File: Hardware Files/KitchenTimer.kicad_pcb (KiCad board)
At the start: 2 copper layers, 72.5 x 56 mm, 54 parts, among them J1 Conn_01x04, J2 USB_B_Micro, J3 Mounting Hole, J4 Mounting Hole, J5 Mounting Hole, J6 Mounting Hole, Q1 P 1V 250uA 4A SOT-23, Q2 P 1V 250uA 4A SOT-23, Q3 P 1V 250uA 4A SOT-23, Q4 P 1V 250uA 4A SOT-23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

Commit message: fix shift register pin mapping and routing
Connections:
- U3 pad 14: Data -> ShiftRegister_1_overflow
- U3 pad 9: ShiftRegister_1_overflow -> ShiftRegister_2_overflow
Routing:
- net Data: track 63.8 -> 17.2 mm, vias 2 -> 1
- net ShiftRegister_1_overflow: track 45.8 -> 40.2 mm, vias 2 -> 0
- net GND: track 72.4 -> 75.0 mm, vias 11 -> 12
- net ESP_RX: track 27.9 -> 26.8 mm

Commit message: update layout
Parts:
- R12, R13, R14, R15, R16, R17, R18, R19: value R -> 10Ω 100mW 0603
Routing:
- net (no net): track 0.00 -> 8.74 mm
- net BTN_StartStop: track 97.1 -> 105.0 mm
- net BTN_Down: track 105.8 -> 113.8 mm
- net BTN_Up: track 62.2 -> 70.2 mm
- net BTN_ResetCountdown: track 99.6 -> 107.5 mm
- net +3V3: track 63.0 -> 60.8 mm, vias 10 -> 13
- net ESP_Enable: track 23.9 -> 24.4 mm

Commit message: update components
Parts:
- C10, C12: value 220nF 50V -> 220nF
- C13, C9: value 10uF ±10% 25V X5R -> 10uF
- J1: value Conn_01x04 -> 2.54mm 1x4
- J2: value USB_B_Micro -> MicroUSB
- R12, R13, R14, R15, R16, R17, R18, R19: value 10Ω 100mW 0603 -> 10Ω
- SW1, SW2: value SW_SPST -> SPST
- SW3, SW4, SW5, SW6: value SW_Push_Dual -> SPST
- U2, U3: value 74HC595 -> Serial to Parallel Shift Register
- U4: value NCP1117ST33T3G -> 3.3 V Linear Regulator

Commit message: finalize layout
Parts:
- added G***: LOGO, .[--Stasis.Footprints.Library:PCBA Revision, B.Cu at (33.0, 70.8)
- added R20: 10Ω, Resistor_SMD:R_0603_1608Metric_Pad0.98x0.95mm_HandSolder, B.Cu at (63.0, 45.5)
- moved R18 5.00 mm to (63.0, 59.5)
- moved R14 4.80 mm to (63.0, 57.8)
- moved R19 4.60 mm to (63.0, 56.0)
- moved R15 4.41 mm to (63.0, 54.2)
- moved R16 4.22 mm to (63.0, 52.5)
- moved R12 4.03 mm to (63.0, 50.8)
- moved R17 3.85 mm to (63.0, 49.0)
- moved R13 3.67 mm to (63.0, 47.2)
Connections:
- LED1 pad 8: GND -> Net-(LED1-Pad8)
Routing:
- net +3V3: track 60.8 -> 51.6 mm, vias 13 -> 15
- net Net-(LED1-Pad8): track 0.00 -> 7.07 mm
- net Net-(LED1-Pad13): track 19.0 -> 24.3 mm
- net Net-(LED1-Pad12): track 15.3 -> 20.1 mm
- net Net-(LED1-Pad9): track 6.41 -> 10.8 mm
- net BTN_ResetCountdown: track 107.5 -> 111.2 mm
- net GND: track 75.0 -> 71.4 mm, vias 12 -> 15
- net LED_G: track 32.0 -> 34.4 mm
- net LED_C: track 21.6 -> 23.8 mm
- net LED_B: track 5.11 -> 7.32 mm
- net LED_DP: track 18.6 -> 20.7 mm
- net Net-(LED1-Pad5): track 9.46 -> 11.3 mm
- net LED_F: track 7.75 -> 9.60 mm
- net LED_A: track 10.4 -> 12.2 mm
- net LED_D: track 16.0 -> 17.8 mm
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- added copper zone on F.Cu, net +3V3
- added copper zone on B.Cu, net GND
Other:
- board text added: "5 V"
- board text added: "BOOT"
- board text added: "DOWN"
- board text added: "EN"
- board text added: "GND"
- board text added: "HR"
- board text added: "MIN"
- board text added: "RESET"
- board text added: "RX"
- board text added: "START"
- board text added: "STOP"
- board text added: "TIMER"
- board text added: "TX"
- board text added: "UP"

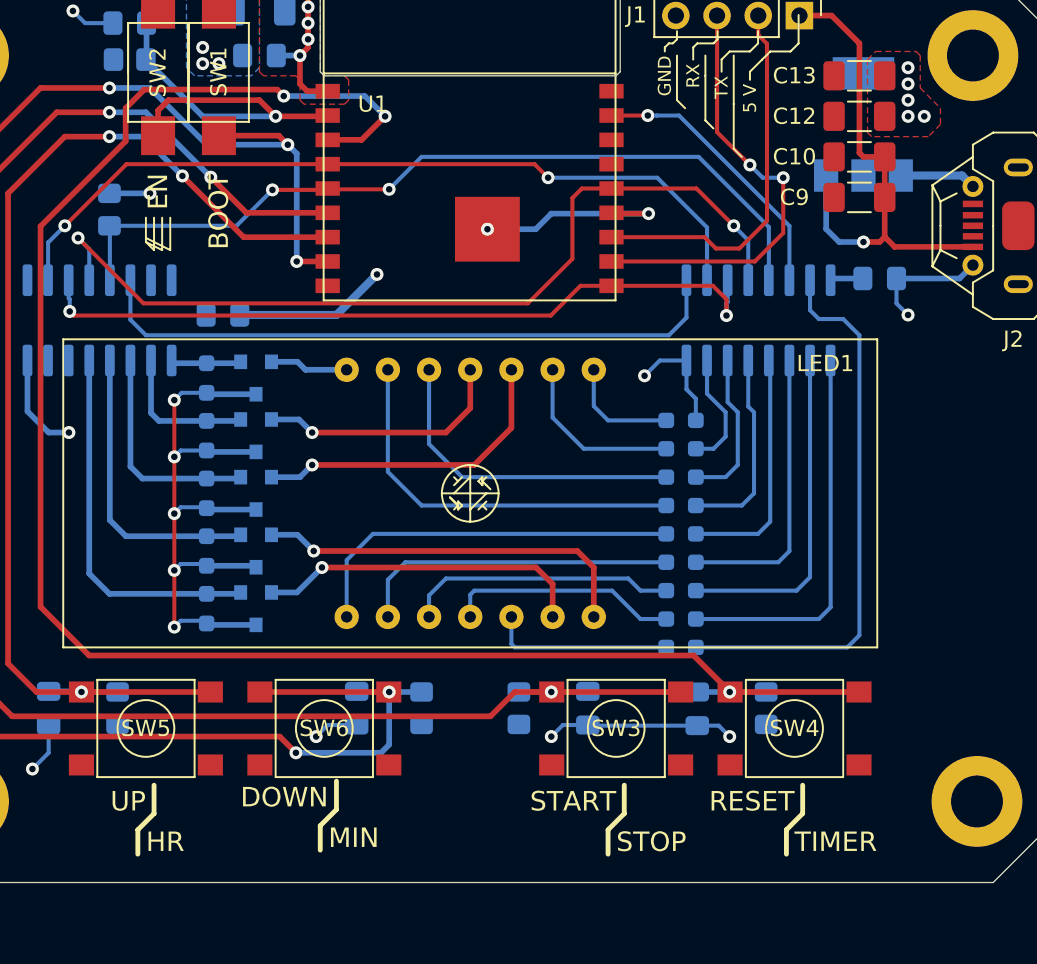
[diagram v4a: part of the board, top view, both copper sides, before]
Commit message: finalize silkscreen layers
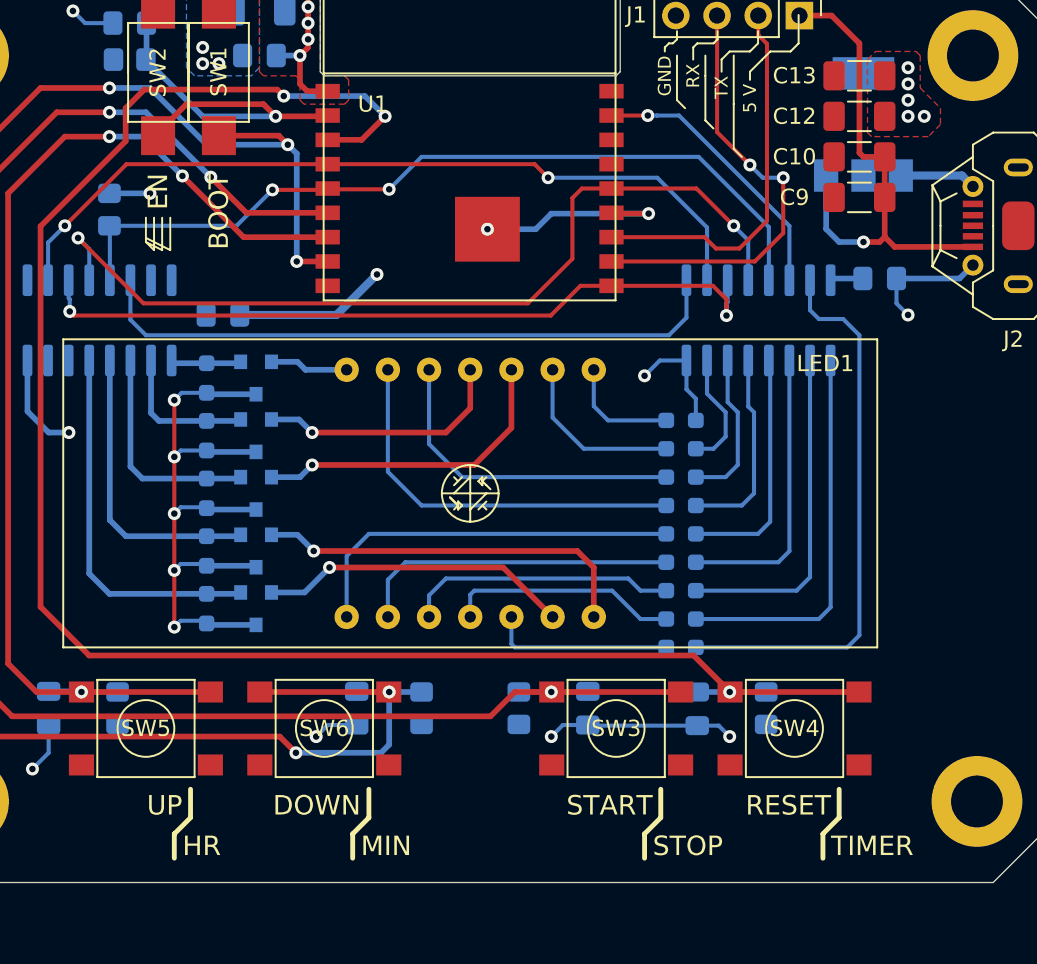
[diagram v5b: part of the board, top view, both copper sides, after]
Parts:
- added G***: LOGO, .[--Stasis.Footprints.Logos:Stasis_Logo_25mm_7mm, B.Cu at (50.0, 29.8)
- added G***: LOGO, .[--Stasis.Footprints.Logos:Order_Number_25.6mm_5mm, B.Cu at (63.2, 70.5)
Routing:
- net Char_4_Power: track 20.4 -> 19.2 mm
- net ESP_Enable: track 24.4 -> 23.4 mm
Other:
- board text added: "Kitchen Timer"
